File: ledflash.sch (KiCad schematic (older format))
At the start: 12 parts

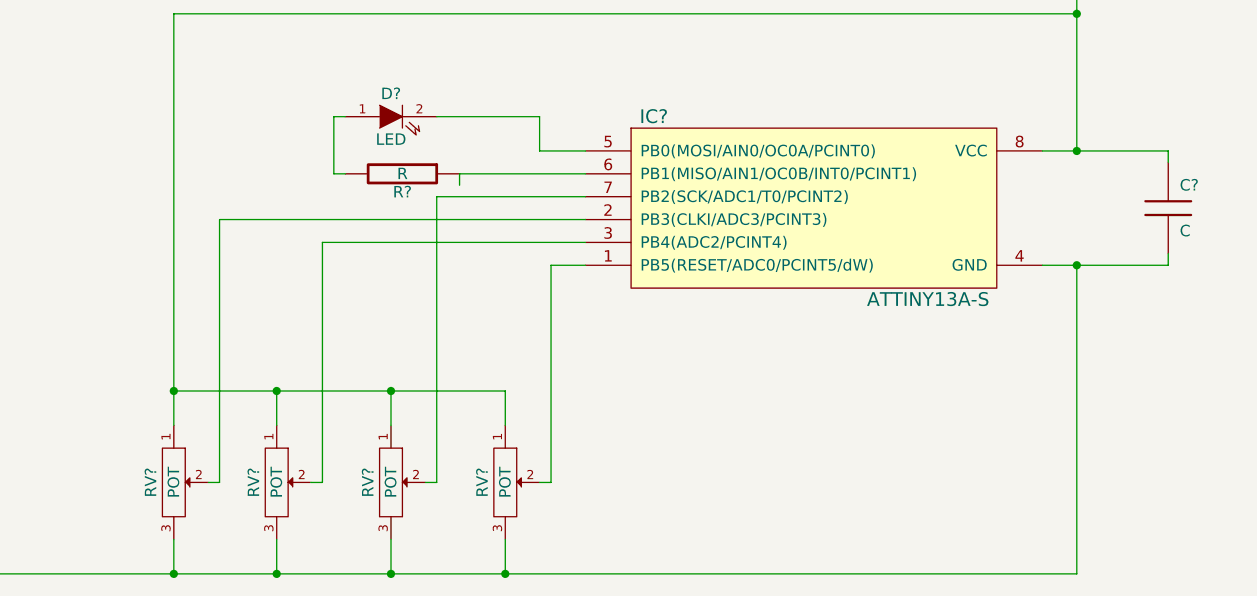
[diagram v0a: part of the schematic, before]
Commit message: Component values
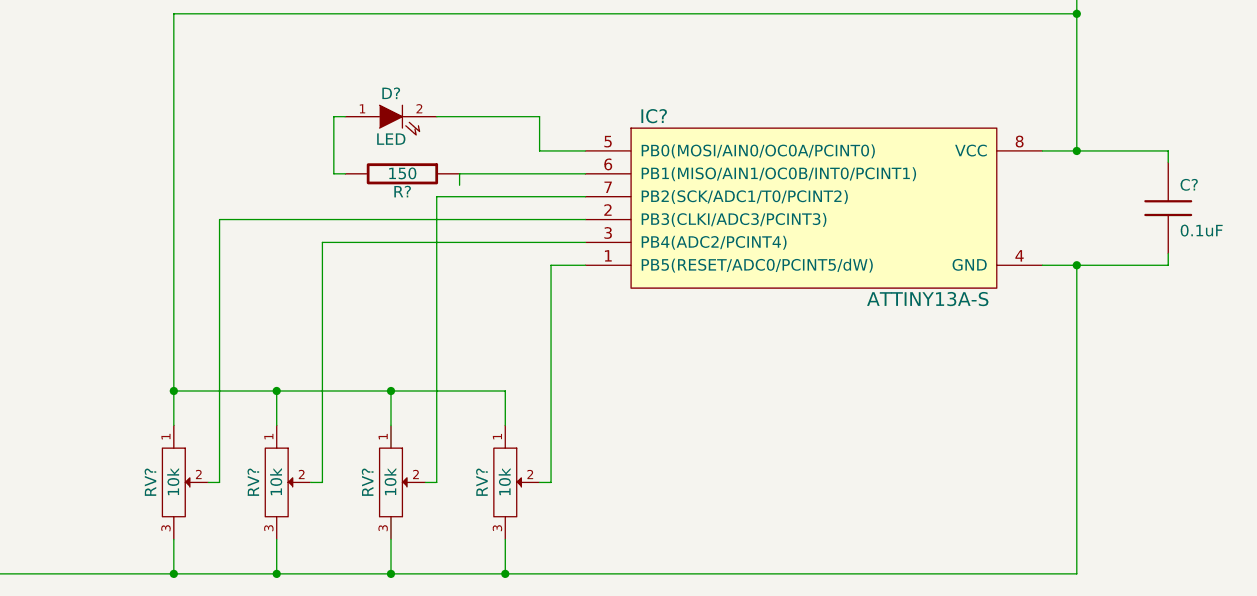
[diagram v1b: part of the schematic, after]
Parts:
- C?: value C -> 0.1uF
- R?: value R -> 150
- RV? (x4): value POT -> 10k
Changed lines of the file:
@@
-EESchema Schematic File Version 2  date Tue 03 Dec 2013 13:59:40 EST
+EESchema Schematic File Version 2  date Tue 03 Dec 2013 14:15:26 EST
 LIBS:power
 LIBS:device
@@
 LIBS:contrib
 LIBS:valves
-EELAYER 43  0
+LIBS:ledflash-cache
+EELAYER 24  0
 EELAYER END
 $Descr A4 11700 8267
@@
 P 7800 4100
 F 0 "C?" H 7850 4200 50  0000 L CNN
-F 1 "C" H 7850 4000 50  0000 L CNN
+F 1 "0.1uF" H 7850 4000 50  0000 L CNN
 	1    7800 4100
 	1    0    0    -1
@@
 P 4450 3950
 F 0 "R?" V 4530 3950 50  0000 C CNN
-F 1 "R" V 4450 3950 50  0000 C CNN
+F 1 "150" V 4450 3950 50  0000 C CNN
 	1    4450 3950
 	0    1    1    0
@@
 P 3450 5300
 F 0 "RV?" H 3450 5200 50  0000 C CNN
-F 1 "POT" H 3450 5300 50  0000 C CNN
+F 1 "10k" H 3450 5300 50  0000 C CNN
 	1    3450 5300
 	0    1    1    0
@@
 P 3900 5300
 F 0 "RV?" H 3900 5200 50  0000 C CNN
-F 1 "POT" H 3900 5300 50  0000 C CNN
+F 1 "10k" H 3900 5300 50  0000 C CNN
 	1    3900 5300
 	0    1    1    0
@@
 P 4400 5300
 F 0 "RV?" H 4400 5200 50  0000 C CNN
-F 1 "POT" H 4400 5300 50  0000 C CNN
+F 1 "10k" H 4400 5300 50  0000 C CNN
 	1    4400 5300
 	0    1    1    0
@@
 P 4900 5300
 F 0 "RV?" H 4900 5200 50  0000 C CNN
-F 1 "POT" H 4900 5300 50  0000 C CNN
+F 1 "10k" H 4900 5300 50  0000 C CNN
 	1    4900 5300
 	0    1    1    0

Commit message: power connector added
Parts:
- added P?: CONN_2, symbol CONN_2
- C? (x2): value C -> 10uF
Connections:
- net at D?.2: now also P?.1 (P1)
- net at D?.4: now also P?.2 (PM)
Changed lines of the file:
@@
-EESchema Schematic File Version 2  date Tue 03 Dec 2013 14:15:26 EST
+EESchema Schematic File Version 2  date Tue 03 Dec 2013 14:17:17 EST
 LIBS:power
 LIBS:device
@@
 Comment4 ""
 $EndDescr
+Wire Wire Line
+	2250 2950 2250 3000
+Wire Wire Line
+	2250 3000 1050 3000
+Wire Wire Line
+	1050 3000 1050 1350
 Connection ~ 4950 2100
 Wire Wire Line
@@
 	4950 3100 1300 3100
 Connection ~ 4200 3100
+Wire Wire Line
+	1050 1150 2250 1150
+Wire Wire Line
+	2250 1150 2250 1250
+$Comp
+L CONN_2 P?
+U 1 1 529D4D0C
+P 700 1250
+F 0 "P?" V 650 1250 40  0000 C CNN
+F 1 "CONN_2" V 750 1250 40  0000 C CNN
+	1    700  1250
+	-1   0    0    1
+$EndComp
 $Comp
 L C C?
@@
 P 4950 2650
 F 0 "C?" H 5000 2750 50  0000 L CNN
-F 1 "C" H 5000 2550 50  0000 L CNN
+F 1 "10uF" H 5000 2550 50  0000 L CNN
 	1    4950 2650
 	1    0    0    -1
@@
 P 3400 2600
 F 0 "C?" H 3450 2700 50  0000 L CNN
-F 1 "C" H 3450 2500 50  0000 L CNN
+F 1 "10uF" H 3450 2500 50  0000 L CNN
 	1    3400 2600
 	1    0    0    -1
